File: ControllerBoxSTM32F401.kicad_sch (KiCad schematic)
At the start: 22 parts, among them J1 Conn_01x05_Male, J2 Conn_01x04_Male, U1 YAAJ_WeAct_BlackPill_Part_Lik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

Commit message: change component to SMD, and lowering the footprint to <100mm
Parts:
- C1, C2, C3, C4, C5, C6: footprint Capacitor_THT:C_Radial_D6.3mm_H7.0mm_P2.50mm -> Capacitor_SMD:C_0805_2012Metric_Pad1.18x1.45mm_HandSolder
- R1, R2, R3, R4, R5, R6, R7, R8, R9: footprint Resistor_THT:R_Box_L8.4mm_W2.5mm_P5.08mm -> Resistor_SMD:R_0805_2012Metric_Pad1.20x1.40mm_HandSolder
- U1: footprint YAAJ_WeAct_BlackPill_SWD_2 -> YAAJ_WeAct_BlackPill_2

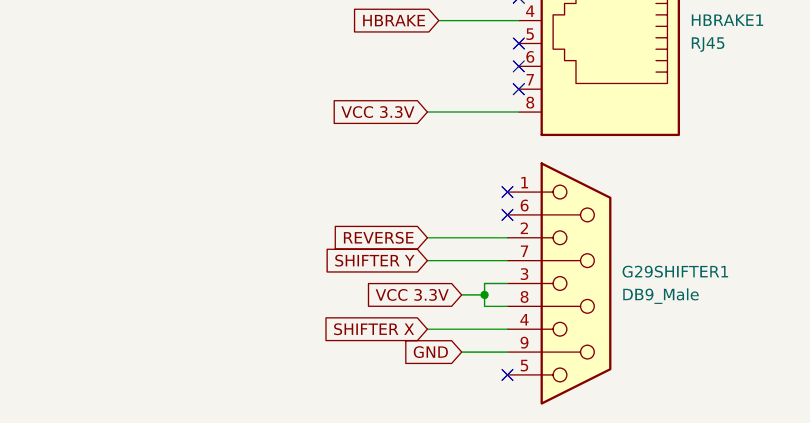
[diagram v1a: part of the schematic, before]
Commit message: add readme; fix wrong pin issue for G29Shifter
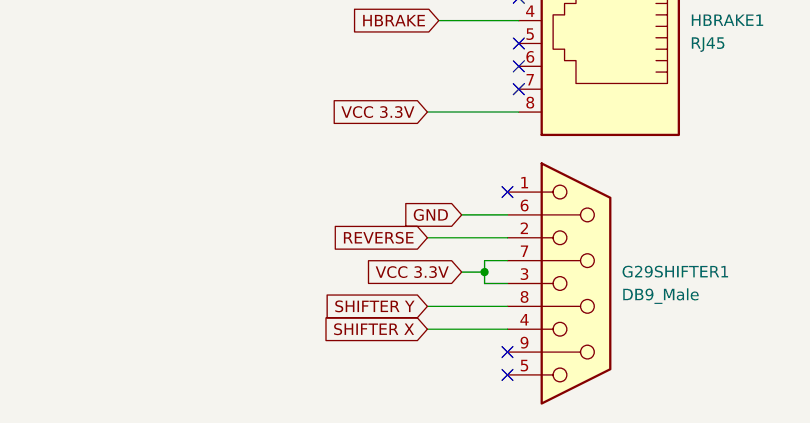
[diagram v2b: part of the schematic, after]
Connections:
- net GND: now also G29SHIFTER1.6; no longer G29SHIFTER1.9
- net SHIFTER Y: now also G29SHIFTER1.8; no longer G29SHIFTER1.7
- net VCC 3.3V: now also G29SHIFTER1.7; no longer G29SHIFTER1.8
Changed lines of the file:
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@@
   (junction (at 166.37 85.09) (diameter 0) (color 0 0 0 0)
   )
-  (junction (at 243.84 127) (diameter 0) (color 0 0 0 0)
-  )
   (junction (at 166.37 54.61) (diameter 0) (color 0 0 0 0)
   )
@@
   )
   (junction (at 171.45 72.39) (diameter 0) (color 0 0 0 0)
+  )
+  (junction (at 243.84 124.46) (diameter 0) (color 0 0 0 0)
   )
   (junction (at 160.02 57.15) (diameter 0) (color 0 0 0 0)
@@
   (no_connect (at 247.65 91.44))
   (no_connect (at 246.38 115.57))
-  (no_connect (at 246.38 118.11))
+  (no_connect (at 246.38 133.35))
   (no_connect (at 246.38 135.89))
   (no_connect (at 101.6 85.09))
@@
   (no_connect (at 147.32 67.31))
   (no_connect (at 147.32 64.77))
+  (wire (pts (xy 243.84 123.19) (xy 246.38 123.19))
+    (stroke (width 0) (type default) (color 0 0 0 0))
+  )
   (wire (pts (xy 156.21 57.15) (xy 156.21 74.93))
     (stroke (width 0) (type default) (color 0 0 0 0))
@@
     (stroke (width 0) (type default) (color 0 0 0 0))
   )
+  (wire (pts (xy 243.84 124.46) (xy 243.84 123.19))
+    (stroke (width 0) (type default) (color 0 0 0 0))
+  )
   (wire (pts (xy 147.32 87.63) (xy 158.75 87.63))
     (stroke (width 0) (type default) (color 0 0 0 0))
   )
-  (wire (pts (xy 237.49 123.19) (xy 246.38 123.19))
-    (stroke (width 0) (type default) (color 0 0 0 0))
-  )
   (wire (pts (xy 237.49 40.64) (xy 247.65 40.64))
     (stroke (width 0) (type default) (color 0 0 0 0))
@@
     (stroke (width 0) (type default) (color 0 0 0 0))
   )
+  (wire (pts (xy 243.84 124.46) (xy 243.84 125.73))
+    (stroke (width 0) (type default) (color 0 0 0 0))
+  )
   (wire (pts (xy 152.4 67.31) (xy 152.4 90.17))
     (stroke (width 0) (type default) (color 0 0 0 0))
@@
     (stroke (width 0) (type default) (color 0 0 0 0))
   )
+  (wire (pts (xy 241.3 124.46) (xy 243.84 124.46))
+    (stroke (width 0) (type default) (color 0 0 0 0))
+  )
   (wire (pts (xy 237.49 50.8) (xy 247.65 50.8))
     (stroke (width 0) (type default) (color 0 0 0 0))
   )
+  (wire (pts (xy 237.49 128.27) (xy 246.38 128.27))
+    (stroke (width 0) (type default) (color 0 0 0 0))
+  )
   (wire (pts (xy 237.49 63.5) (xy 247.65 63.5))
     (stroke (width 0) (type default) (color 0 0 0 0))
@@
     (stroke (width 0) (type default) (color 0 0 0 0))
   )
-  (wire (pts (xy 241.3 133.35) (xy 246.38 133.35))
+  (wire (pts (xy 241.3 118.11) (xy 246.38 118.11))
     (stroke (width 0) (type default) (color 0 0 0 0))
   )
@@
     (stroke (width 0) (type default) (color 0 0 0 0))
   )
-  (wire (pts (xy 241.3 127) (xy 243.84 127))
-    (stroke (width 0) (type default) (color 0 0 0 0))
-  )
   (wire (pts (xy 171.45 64.77) (xy 171.45 57.15))
     (stroke (width 0) (type default) (color 0 0 0 0))
@@
     (stroke (width 0) (type default) (color 0 0 0 0))
   )
-  (wire (pts (xy 243.84 127) (xy 243.84 128.27))
-    (stroke (width 0) (type default) (color 0 0 0 0))
-  )
-  (wire (pts (xy 243.84 128.27) (xy 246.38 128.27))
-    (stroke (width 0) (type default) (color 0 0 0 0))
-  )
   (wire (pts (xy 237.49 38.1) (xy 247.65 38.1))
     (stroke (width 0) (type default) (color 0 0 0 0))
@@
   )
   (wire (pts (xy 237.49 130.81) (xy 246.38 130.81))
-    (stroke (width 0) (type default) (color 0 0 0 0))
-  )
-  (wire (pts (xy 243.84 125.73) (xy 243.84 127))
     (stroke (width 0) (type default) (color 0 0 0 0))
   )
@@
     )
   )
-  (global_label "GND" (shape input) (at 241.3 133.35 180) (fields_autoplaced)
-    (effects (font (size 1.27 1.27)) (justify right))
-    (property "Intersheet References" "${INTERSHEET_REFS}" (id 0) (at 235.0164 133.2706 0)
-      (effects (font (size 1.27 1.27)) (justify right) hide)
-    )
-  )
-  (global_label "SHIFTER Y" (shape input) (at 237.49 123.19 180) (fields_autoplaced)
-    (effects (font (size 1.27 1.27)) (justify right))
-    (property "Intersheet References" "${INTERSHEET_REFS}" (id 0) (at 225.4007 123.1106 0)
+  (global_label "GND" (shape input) (at 241.3 118.11 180) (fields_autoplaced)
+    (effects (font (size 1.27 1.27)) (justify right))
+    (property "Intersheet References" "${INTERSHEET_REFS}" (id 0) (at 235.0164 118.0306 0)
+      (effects (font (size 1.27 1.27)) (justify right) hide)
+    )
+  )
+  (global_label "SHIFTER Y" (shape input) (at 237.49 128.27 180) (fields_autoplaced)
+    (effects (font (size 1.27 1.27)) (justify right))
+    (property "Intersheet References" "${INTERSHEET_REFS}" (id 0) (at 225.4007 128.1906 0)
       (effects (font (size 1.27 1.27)) (justify right) hide)
     )
@@
     )
   )
-  (global_label "VCC 3.3V" (shape input) (at 241.3 127 180) (fields_autoplaced)
-    (effects (font (size 1.27 1.27)) (justify right))
-    (property "Intersheet References" "${INTERSHEET_REFS}" (id 0) (at 230.1783 126.9206 0)
-      (effects (font (size 1.27 1.27)) (justify right) hide)
-    )
+  (global_label "VCC 3.3V" (shape input) (at 241.3 124.46 180) (fields_autoplaced)
+    (effects (font (size 1.27 1.27)) (justify right))
+    (property "Intersheet References" "${INTERSHEET_REFS}" (id 0) (at 230.1783 124.3806 0)
+      (effects (font (size 1.27 1.27)) (justify right) hide)
+    )
